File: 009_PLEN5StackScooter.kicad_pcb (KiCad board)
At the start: 2 copper layers, 0 parts

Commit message: [Add]インジケータLED追加
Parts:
- added BT1: Battery_Cell, 00_DIY_MyFavorite:BatteryHolder_BX123P38, F.Cu at (79.1, 61.2)
- added IC1: TB6608FNG_O,EL_, 01_AddLibrary:SOP65P640X160-20N, F.Cu at (80.6, 75.0)
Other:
- board outline added: 49.8 x 32 mm
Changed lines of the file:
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@@
   )
   (net 0 "")
+  (net 1 "+BATT")
+  (net 2 "GND")
+  (net 3 "VCC")
+  (net 4 "Standby")
+  (net 5 "Net-(IC1-OSC)")
+  (net 6 "Direction")
+  (net 7 "MotorB2")
+  (net 8 "Net-(IC1-RFB)")
+  (net 9 "MotorB1")
+  (net 10 "MotorA2")
+  (net 11 "Net-(IC1-RFA)")
+  (net 12 "MotorA1")
+  (net 13 "Reset")
+  (net 14 "unconnected-(IC1-~{MO}-Pad16)")
+  (net 15 "Enable")
+  (net 16 "Clock")
+  (footprint "00_DIY_MyFavorite:BatteryHolder_BX123P38" (layer "F.Cu")
+    (at 79.094 61.214)
+    (property "Sheetfile" "009_PLEN5StackScooter.kicad_sch")
+    (property "Sheetname" "")
+    (property "ki_description" "Single-cell battery")
+    (property "ki_keywords" "battery cell")
+    (attr through_hole)
+    (fp_text reference "BT1" (at 19 0 unlocked) (layer "F.SilkS")
+        (effects (font (size 1 1) (thickness 0.15)))
+    )
+    (fp_text value "Battery_Cell" (at 19 4 unlocked) (layer "F.Fab")
+        (effects (font (size 1 1) (thickness 0.15)))
+    )
+    (fp_text user "-" (at 35 -1 unlocked) (layer "F.SilkS")
+        (effects (font (size 1.5 1.5) (thickness 0.15)) (justify left bottom))
+    )
+    (fp_text user "+" (at 1 -1 unlocked) (layer "F.SilkS")
+        (effects (font (size 1.5 1.5) (thickness 0.15)) (justify left bottom))
+    )
+    (fp_rect (start -2.4 -9) (end 40.4 9)
+      (stroke (width 0.12) (type default)) (fill none) (layer "F.SilkS"))
+    (fp_circle (center 0 -8.2) (end 0.9 -8.2)
+      (stroke (width 0.12) (type default)) (fill none) (layer "Edge.Cuts"))
+    (pad "1" thru_hole circle (at 0 0) (size 2 2) (drill 1.4) (layers "*.Cu" "*.Mask")
+      (net 1 "+BATT") (pinfunction "+") (pintype "passive"))
+    (pad "2" thru_hole circle (at 38 0) (size 2 2) (drill 1.4) (layers "*.Cu" "*.Mask")
+      (net 2 "GND") (pinfunction "-") (pintype "passive"))
+    (model ":LIB:00_DIY_MyFavorite/3dmodels/BatteryHolder_BX123P38.STEP"
+      (offset (xyz 0 0 0))
+      (scale (xyz 1 1 1))
+      (rotate (xyz -90 0 0))
+    )
+  )
+  (footprint "01_AddLibrary:SOP65P640X160-20N" (layer "F.Cu")
+    (at 80.634 75.049)
+    (descr "SSOP20-P-225-0.65A")
+    (tags "Integrated Circuit")
+    (property "Height" "1.6")
+    (property "Manufacturer_Name" "Toshiba")
+    (property "Manufacturer_Part_Number" "TB6608FNG(O,EL)")
+    (property "RS Part Number" "")
+    (property "RS Price/Stock" "")
+    (property "Sheetfile" "009_PLEN5StackScooter.kicad_sch")
+    (property "Sheetname" "")
+    (property "ki_description" "Motor / Motion / Ignition Controllers & Drivers Stepping Motor Driver")
+    (attr smd)
+    (fp_text reference "IC1" (at 0 0) (layer "F.SilkS")
+        (effects (font (size 1.27 1.27) (thickness 0.254)))
+    )
+    (fp_text value "TB6608FNG_O,EL_" (at 0 0) (layer "F.SilkS") hide
+        (effects (font (size 1.27 1.27) (thickness 0.254)))
+    )
+    (fp_text user "${REFERENCE}" (at 0 0) (layer "F.Fab")
+        (effects (font (size 1.27 1.27) (thickness 0.254)))
+    )
+    (fp_line (start -3.725 -3.5) (end -2.2 -3.5)
+      (stroke (width 0.2) (type solid)) (layer "F.SilkS"))
+    (fp_line (start -1.85 -3.5) (end 1.85 -3.5)
+      (stroke (width 0.2) (type solid)) (layer "F.SilkS"))
+    (fp_line (start -1.85 3.5) (end -1.85 -3.5)
+      (stroke (width 0.2) (type solid)) (layer "F.SilkS"))
+    (fp_line (start 1.85 -3.5) (end 1.85 3.5)
+      (stroke (width 0.2) (type solid)) (layer "F.SilkS"))
+    (fp_line (start 1.85 3.5) (end -1.85 3.5)
+      (stroke (width 0.2) (type solid)) (layer "F.SilkS"))
+    (fp_line (start -3.975 -3.75) (end 3.975 -3.75)
+      (stroke (width 0.05) (type solid)) (layer "F.CrtYd"))
+    (fp_line (start -3.975 3.75) (end -3.975 -3.75)
+      (stroke (width 0.05) (type solid)) (layer "F.CrtYd"))
+    (fp_line (start 3.975 -3.75) (end 3.975 3.75)
+      (stroke (width 0.05) (type solid)) (layer "F.CrtYd"))
+    (fp_line (start 3.975 3.75) (end -3.975 3.75)
+      (stroke (width 0.05) (type solid)) (layer "F.CrtYd"))
+    (fp_line (start -2.2 -3.5) (end 2.2 -3.5)
+      (stroke (width 0.1) (type solid)) (layer "F.Fab"))
+    (fp_line (start -2.2 -2.85) (end -1.55 -3.5)
+      (stroke (width 0.1) (type solid)) (layer "F.Fab"))
+    (fp_line (start -2.2 3.5) (end -2.2 -3.5)
+      (stroke (width 0.1) (type solid)) (layer "F.Fab"))
+    (fp_line (start 2.2 -3.5) (end 2.2 3.5)
+      (stroke (width 0.1) (type solid)) (layer "F.Fab"))
+    (fp_line (start 2.2 3.5) (end -2.2 3.5)
+      (stroke (width 0.1) (type solid)) (layer "F.Fab"))
+    (pad "1" smd rect (at -2.962 -2.925 90) (size 0.45 1.525) (layers "F.Cu" "F.Paste" "F.Mask")
+      (net 3 "VCC") (pinfunction "VCC") (pintype "passive"))
+    (pad "2" smd rect (at -2.962 -2.275 90) (size 0.45 1.525) (layers "F.Cu" "F.Paste" "F.Mask")
+      (net 4 "Standby") (pinfunction "STBY") (pintype "passive"))
+    (pad "3" smd rect (at -2.962 -1.625 90) (size 0.45 1.525) (layers "F.Cu" "F.Paste" "F.Mask")
+      (net 5 "Net-(IC1-OSC)") (pinfunction "OSC") (pintype "passive"))
+    (pad "4" smd rect (at -2.962 -0.975 90) (size 0.45 1.525) (layers "F.Cu" "F.Paste" "F.Mask")
+      (net 3 "VCC") (pinfunction "M1") (pintype "passive"))
+    (pad "5" smd rect (at -2.962 -0.325 90) (size 0.45 1.525) (layers "F.Cu" "F.Paste" "F.Mask")
+      (net 2 "GND") (pinfunction "M2") (pintype "passive"))
+    (pad "6" smd rect (at -2.962 0.325 90) (size 0.45 1.525) (layers "F.Cu" "F.Paste" "F.Mask")
+      (net 1 "+BATT") (pinfunction "VM") (pintype "passive"))
+    (pad "7" smd rect (at -2.962 0.975 90) (size 0.45 1.525) (layers "F.Cu" "F.Paste" "F.Mask")
+      (net 6 "Direction") (pinfunction "CW/CCW") (pintype "passive"))
+    (pad "8" smd rect (at -2.962 1.625 90) (size 0.45 1.525) (layers "F.Cu" "F.Paste" "F.Mask")
+      (net 7 "MotorB2") (pinfunction "BO2") (pintype "passive"))
+    (pad "9" smd rect (at -2.962 2.275 90) (size 0.45 1.525) (layers "F.Cu" "F.Paste" "F.Mask")
+      (net 8 "Net-(IC1-RFB)") (pinfunction "RFB") (pintype "passive"))
+    (pad "10" smd rect (at -2.962 2.925 90) (size 0.45 1.525) (layers "F.Cu" "F.Paste" "F.Mask")
+      (net 9 "MotorB1") (pinfunction "BO1") (pintype "passive"))
+    (pad "11" smd rect (at 2.962 2.925 90) (size 0.45 1.525) (layers "F.Cu" "F.Paste" "F.Mask")
+      (net 10 "MotorA2") (pinfunction "AO2") (pintype "passive"))
+    (pad "12" smd rect (at 2.962 2.275 90) (size 0.45 1.525) (layers "F.Cu" "F.Paste" "F.Mask")
+      (net 11 "Net-(IC1-RFA)") (pinfunction "RFA") (pintype "passive"))
+    (pad "13" smd rect (at 2.962 1.625 90) (size 0.45 1.525) (layers "F.Cu" "F.Paste" "F.Mask")
+      (net 12 "MotorA1") (pinfunction "AO1") (pintype "passive"))
+    (pad "14" smd rect (at 2.962 0.975 90) (size 0.45 1.525) (layers "F.Cu" "F.Paste" "F.Mask")
+      (net 13 "Reset") (pinfunction "RESET") (pintype "passive"))
+    (pad "15" smd rect (at 2.962 0.325 90) (size 0.45 1.525) (layers "F.Cu" "F.Paste" "F.Mask")
+      (net 2 "GND") (pinfunction "GND") (pintype "passive"))
+    (pad "16" smd rect (at 2.962 -0.325 90) (size 0.45 1.525) (layers "F.Cu" "F.Paste" "F.Mask")
+      (net 14 "unconnected-(IC1-~{MO}-Pad16)") (pinfunction "~{MO}") (pintype "passive+no_connect"))
+    (pad "17" smd rect (at 2.962 -0.975 90) (size 0.45 1.525) (layers "F.Cu" "F.Paste" "F.Mask")
+      (net 2 "GND") (pinfunction "TQ") (pintype "passive"))
+    (pad "18" smd rect (at 2.962 -1.625 90) (size 0.45 1.525) (layers "F.Cu" "F.Paste" "F.Mask")
+      (net 2 "GND") (pinfunction "DCY") (pintype "passive"))
+    (pad "19" smd rect (at 2.962 -2.275 90) (size 0.45 1.525) (layers "F.Cu" "F.Paste" "F.Mask")
+      (net 15 "Enable") (pinfunction "ENABLE") (pintype "passive"))
+    (pad "20" smd rect (at 2.962 -2.925 90) (size 0.45 1.525) (layers "F.Cu" "F.Paste" "F.Mask")
+      (net 16 "Clock") (pinfunction "CK") (pintype "passive"))
+    (model ":LIB:PCBL/SamacSys_Parts.3dshapes/TB6608FNG,C8,EL.stp"
+      (offset (xyz 0 0 0))
+      (scale (xyz 1 1 1))
+      (rotate (xyz 0 0 0))
+    )
+  )
+  (gr_rect (start 73.914 50.038) (end 123.698 82.042)
+    (stroke (width 0.1) (type default)) (fill none) (layer "Edge.Cuts"))
 )

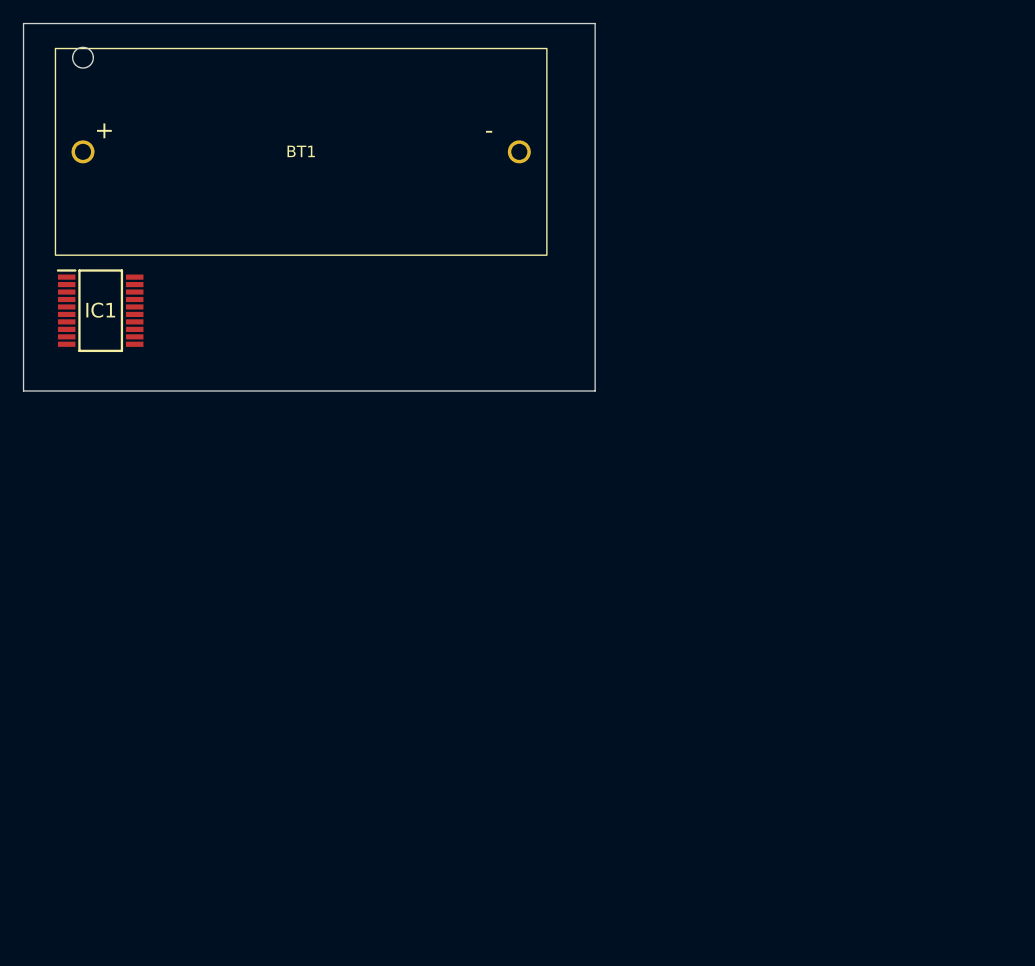
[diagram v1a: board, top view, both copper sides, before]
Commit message: [Add]モータ2台分のドライバIC追加
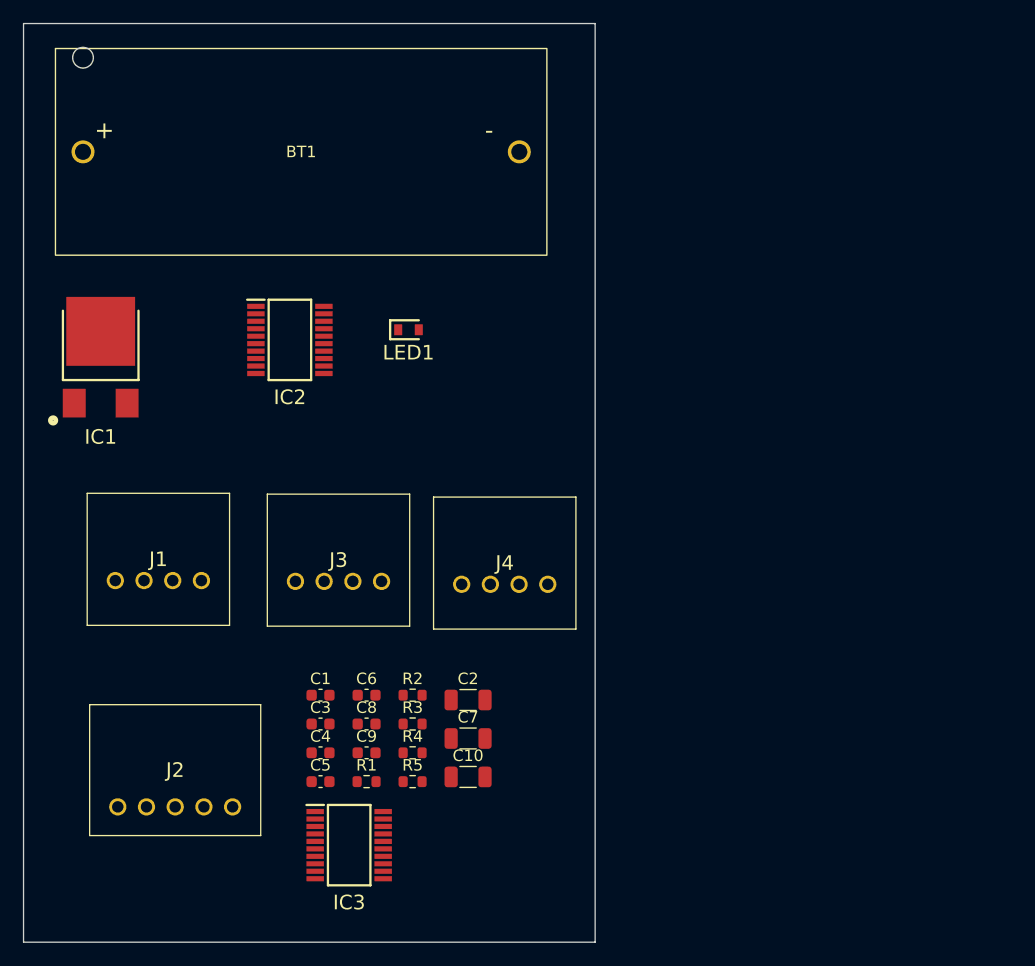
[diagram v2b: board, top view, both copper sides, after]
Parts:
- added C1: 0.1u, Capacitor_SMD:C_0603_1608Metric, F.Cu at (99.8, 108.5)
- added C10: 100u, Capacitor_SMD:C_1206_3216Metric, F.Cu at (112.6, 115.7)
- added C2: 100u, Capacitor_SMD:C_1206_3216Metric, F.Cu at (112.6, 109.0)
- added C3: 0.33u, Capacitor_SMD:C_0603_1608Metric, F.Cu at (99.8, 111.0)
- added C4: 2.2u, Capacitor_SMD:C_0603_1608Metric, F.Cu at (99.8, 113.6)
- added C5: C, Capacitor_SMD:C_0603_1608Metric, F.Cu at (99.8, 116.1)
- added C6: 0.1u, Capacitor_SMD:C_0603_1608Metric, F.Cu at (103.8, 108.5)
- added C7: 100u, Capacitor_SMD:C_1206_3216Metric, F.Cu at (112.6, 112.3)
- added C8: C, Capacitor_SMD:C_0603_1608Metric, F.Cu at (103.8, 111.0)
- added C9: 0.1u, Capacitor_SMD:C_0603_1608Metric, F.Cu at (103.8, 113.6)
- added IC2: TB6608FNG_O,EL_, 01_AddLibrary:SOP65P640X160-20N, F.Cu at (97.1, 77.6)
- added IC3: TB6608FNG_O,EL_, 01_AddLibrary:SOP65P640X160-20N, F.Cu at (102.3, 121.6)
- added J1: S4B-XH-A-1_LF__SN_, 01_AddLibrary:S4BXHA1LFSN, F.Cu at (81.9, 98.6)
- added J2: S5B-XH-A-1_LF__SN_, 01_AddLibrary:S5BXHA1LFSN, F.Cu at (92.1, 118.3)
- added J3: S4B-XH-A-1_LF__SN_, 01_AddLibrary:S4BXHA1LFSN, F.Cu at (97.6, 98.6)
- added J4: S4B-XH-A-1_LF__SN_, 01_AddLibrary:S4BXHA1LFSN, F.Cu at (112.1, 98.9)
- added LED1: SML-E12P8WT86, 01_AddLibrary:LEDC1608X36N, F.Cu at (107.4, 76.7)
- added R1: 1k, Resistor_SMD:R_0603_1608Metric, F.Cu at (103.8, 116.1)
- added R2: 2.2, Resistor_SMD:R_0603_1608Metric, F.Cu at (107.8, 108.5)
- added R3: 2.2, Resistor_SMD:R_0603_1608Metric, F.Cu at (107.8, 111.0)
- added R4: 2.2, Resistor_SMD:R_0603_1608Metric, F.Cu at (107.8, 113.6)
- added R5: 2.2, Resistor_SMD:R_0603_1608Metric, F.Cu at (107.8, 116.1)
- IC1: value TB6608FNG_O,EL_ -> NJM2845DL1-33-TE1; footprint 01_AddLibrary:SOP65P640X160-20N -> 01_AddLibrary:TO-252-3-L1
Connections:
- IC1 pad 1: VCC -> +BATT
- IC1 pad 2: Standby -> +3.3V
- IC1 pad 3: Net-(IC1-OSC) -> GND
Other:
- board size 49.8 x 32 mm -> 49.8 x 80 mm

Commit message: [Add]ステッピングモータテスト用基板設計完
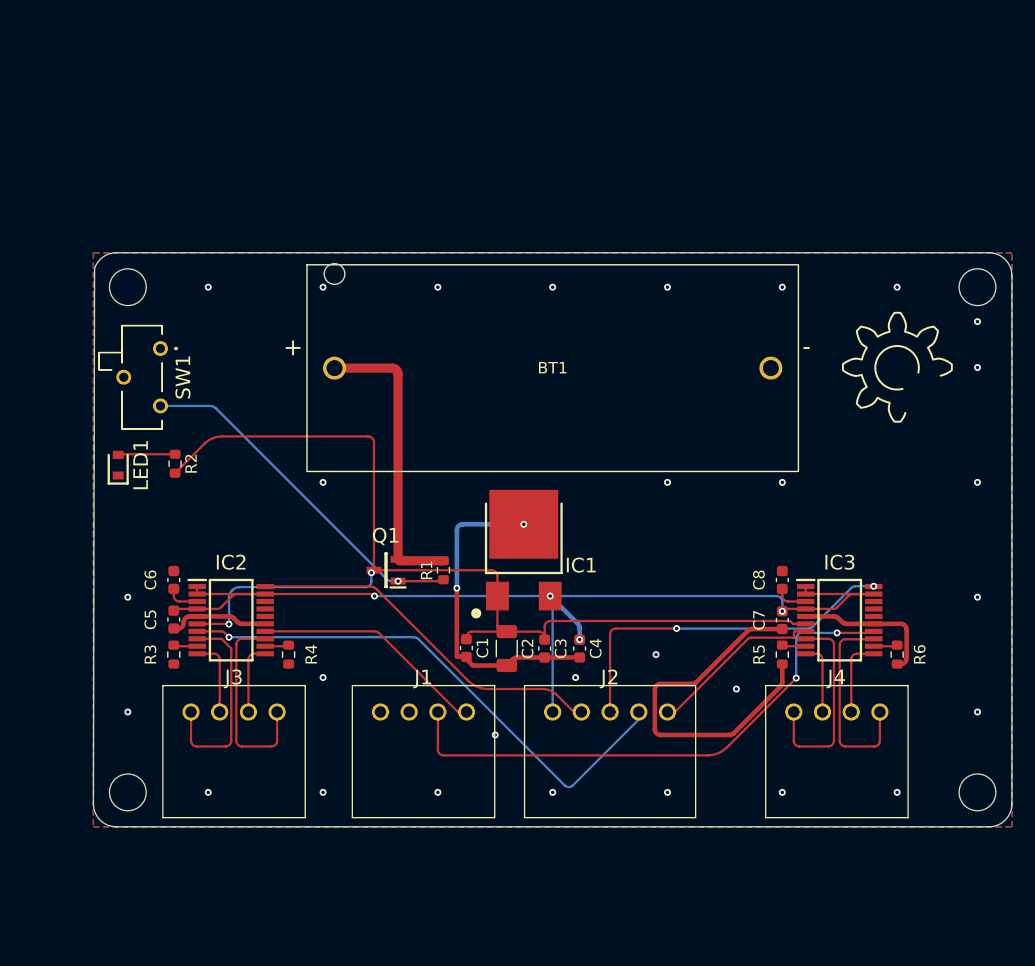
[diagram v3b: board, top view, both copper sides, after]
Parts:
- removed C10: 100u, Capacitor_SMD:C_1206_3216Metric
- removed C9: 0.1u, Capacitor_SMD:C_0603_1608Metric
- added G***: LOGO, 00_DIY_MyFavorite:Symbol_Helical_new, F.Cu at (150.0, 80.0)
- added Q1: IRLML6402, 01_AddLibrary:SOT95P237X112-3N, F.Cu at (105.5, 97.7)
- added R6: 2.2, Resistor_SMD:R_0603_1608Metric, F.Cu at (150.0, 105.0)
- added Ref**: Val**, 10_KBD_Hole_salicylic:m3_Screw_Hole_EdgeCuts, F.Cu at (157.0, 73.0)
- added Ref**: Val**, 10_KBD_Hole_salicylic:m3_Screw_Hole_EdgeCuts, F.Cu at (83.0, 117.0)
- added Ref**: Val**, 10_KBD_Hole_salicylic:m3_Screw_Hole_EdgeCuts, F.Cu at (83.0, 73.0)
- added Ref**: Val**, 10_KBD_Hole_salicylic:m3_Screw_Hole_EdgeCuts, F.Cu at (157.0, 117.0)
- added SW1: SW_OTAX-Toggle, 01_AddLibrary:IS1245TG, F.Cu at (85.8, 78.3)
- C5: value C -> 0.1u
- C6: value 0.1u -> 220p
- C7: value 100u -> 0.1u; footprint Capacitor_SMD:C_1206_3216Metric -> Capacitor_SMD:C_0603_1608Metric
- C8: value C -> 220p
- R2: value 2.2 -> 1k
- moved IC3 47.0 mm to (145.0, 102.0)
- moved IC1 40.5 mm to (117.5, 91.9)
- moved C8 38.3 mm to (140.0, 98.5), turned to 90 degrees
- moved J4 38.1 mm to (148.5, 110.0), turned to 180 degrees
- moved R5 34.0 mm to (140.0, 105.0), turned to -90 degrees
- moved J1 32.7 mm to (112.5, 110.0), turned to 180 degrees
- moved C7 29.2 mm to (140.0, 102.0), turned to -90 degrees
- moved J2 29.1 mm to (120.0, 110.0), turned to 180 degrees
- moved BT1 28.9 mm to (101.0, 80.0)
- moved R2 28.9 mm to (87.1, 88.4), turned to -90 degrees
- moved LED1 27.9 mm to (82.2, 88.5), turned to 90 degrees
- moved IC2 24.9 mm to (92.0, 102.0)
- moved C4 24.3 mm to (122.3, 104.5), turned to -90 degrees
- moved R3 21.7 mm to (87.0, 105.0), turned to -90 degrees
- moved C3 20.6 mm to (119.3, 104.5), turned to -90 degrees
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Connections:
- BT1 pad 1: +BATT -> /Power
- C5 pad 1: Net-(IC2-OSC) -> +3.3V
- C6 pad 1: +3.3V -> Net-(IC2-OSC)
- IC2 pad 17: GND -> unconnected-(IC2-TQ-Pad17)
- IC2 pad 18: GND -> unconnected-(IC2-DCY-Pad18)
- IC2 pad 19: Enable_1 -> +3.3V
- IC2 pad 2: Standby_1 -> +3.3V
- IC3 pad 17: GND -> unconnected-(IC3-TQ-Pad17)
- IC3 pad 18: GND -> unconnected-(IC3-DCY-Pad18)
- IC3 pad 19: Enable_2 -> +3.3V
- IC3 pad 2: Standby_2 -> +3.3V
- J1 pad 1: unconnected-(J1-Pad1) -> Reset_1
- J1 pad 2: unconnected-(J1-Pad2) -> Reset_2
- J1 pad 4: unconnected-(J1-Pad4) -> GND
- J2 pad 1: unconnected-(J2-Pad1) -> +3.3V
- J2 pad 2: unconnected-(J2-Pad2) -> Clock_1
- J2 pad 3: unconnected-(J2-Pad3) -> Clock_2
- J2 pad 4: unconnected-(J2-Pad4) -> Direction_1
- J2 pad 5: unconnected-(J2-Pad5) -> Direction_2
- R1 pad 1: Net-(LED1-A) -> Net-(Q1-G)
- R1 pad 2: +BATT -> /Power
- R2 pad 1: Net-(IC2-RFB) -> Net-(LED1-A)
- R2 pad 2: GND -> +BATT
- R3 pad 1: Net-(IC2-RFA) -> Net-(IC2-RFB)
- R4 pad 1: Net-(IC3-RFB) -> Net-(IC2-RFA)
- R5 pad 1: Net-(IC3-RFA) -> Net-(IC3-RFB)
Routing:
- net +BATT: track 0.00 -> 97.4 mm, vias 0 -> 2
- net +3.3V: track 0.00 -> 91.3 mm, vias 0 -> 4
- net GND: track 0.00 -> 82.3 mm, vias 0 -> 31
- net Reset_2: track 0.00 -> 47.9 mm, vias 0 -> 2
- net Direction_1: track 0.00 -> 47.1 mm, vias 0 -> 1
- net Clock_1: track 0.00 -> 31.8 mm
- net Clock_2: track 0.00 -> 31.5 mm, vias 0 -> 2
- net Net-(Q1-G): track 0.00 -> 30.9 mm, vias 0 -> 1
- net /Power: track 0.00 -> 26.0 mm
- net Reset_1: track 0.00 -> 20.4 mm
- net MotorA3: track 0.00 -> 18.1 mm
- net MotorB2: track 0.00 -> 17.9 mm
- net MotorA1: track 0.00 -> 17.8 mm
- net MotorB4: track 0.00 -> 17.6 mm
- net Direction_2: track 0.00 -> 15.2 mm
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- added copper zone on B.Cu, net GND
- added copper zone on F.Cu, net GND
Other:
- board size 49.8 x 80 mm -> 80 x 50 mm
- board text added: "JLCJLCJLCJLC"
- board text added: "PLEN5StackScooter_TestBoard v1.0"

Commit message: [Add]最終レイアウトに近い基板設計完
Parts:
- removed the Ref** at (157.0, 73.0)
- removed the Ref** at (83.0, 117.0)
- removed the Ref** at (83.0, 73.0)
- removed the Ref** at (157.0, 117.0)
- added D1: CUHS20F30,H3F, 01_AddLibrary:CUHS20F30H3F, F.Cu at (139.0, 78.0)
- added Ref**: Val**, 10_KBD_Hole_salicylic:m3_Screw_Hole_EdgeCuts, F.Cu at (156.0, 116.0)
- added Ref**: Val**, 10_KBD_Hole_salicylic:m3_Screw_Hole_EdgeCuts, F.Cu at (84.0, 64.0)
- added Ref**: Val**, 10_KBD_Hole_salicylic:m3_Screw_Hole_EdgeCuts, F.Cu at (156.0, 64.0)
- added Ref**: Val**, 10_KBD_Hole_salicylic:m3_Screw_Hole_EdgeCuts, F.Cu at (84.0, 116.0)
- moved SW1 57.7 mm to (142.5, 67.2), turned to 180 degrees
- moved LED1 54.6 mm to (131.0, 64.0), turned to 180 degrees
- moved R2 48.4 mm to (131.0, 68.0), turned to 0 degrees
- moved R1 27.9 mm to (107.0, 70.0), turned to 180 degrees
- moved IC1 27.7 mm to (119.0, 64.2)
- moved C3 26.5 mm to (120.0, 78.0)
- moved C4 26.5 mm to (123.0, 78.0)
- moved C2 26.5 mm to (116.0, 78.0)
- moved C1 26.4 mm to (112.0, 78.0)
- moved J4 23.8 mm to (149.6, 86.2), turned to -90 degrees
- moved Q1 21.7 mm to (107.0, 76.0), turned to -90 degrees
- moved J3 17.2 mm to (90.5, 93.8), turned to 90 degrees
- moved BT1 11.0 mm to (101.0, 91.0)
- moved R5 6.40 mm to (145.0, 109.0)
- moved C7 5.83 mm to (145.0, 105.0)
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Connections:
- BT1 pad 2: GND -> Net-(BT1--)
- IC2 pad 17: unconnected-(IC2-TQ-Pad17) -> +3.3V
- IC3 pad 17: unconnected-(IC3-TQ-Pad17) -> +3.3V
- J1 pad 2: Reset_2 -> Direction_1
- J2 pad 4: Direction_1 -> Reset_2
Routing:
- net +3.3V: track 91.3 -> 172.4 mm, vias 4 -> 0
- net GND: track 82.3 -> 40.1 mm, vias 31 -> 32
- net +BATT: track 97.4 -> 125.2 mm, vias 2 -> 3
- net Net-(Q1-G): track 30.9 -> 50.2 mm, vias 1 -> 0
- net MotorA2: track 6.30 -> 23.5 mm, vias 0 -> 1
- net MotorB3: track 6.30 -> 23.4 mm, vias 0 -> 1
- net Net-(BT1--): track 0.00 -> 13.5 mm
- net Direction_1: track 47.1 -> 33.8 mm, vias 1 -> 0
- net MotorA4: track 6.80 -> 20.1 mm, vias 0 -> 1
- net MotorB1: track 6.80 -> 19.5 mm, vias 0 -> 1
- net Reset_2: track 47.9 -> 35.3 mm, vias 2 -> 0
- net Clock_2: track 31.5 -> 41.5 mm, vias 2 -> 0
- net MotorB4: track 17.6 -> 24.9 mm, vias 0 -> 1
- net MotorA1: track 17.8 -> 24.7 mm, vias 0 -> 1
- net Reset_1: track 20.4 -> 13.5 mm
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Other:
- board size 80 x 50 mm -> 80 x 60 mm
- board text added: "PLEN5StackScooter_TestBoard v2.0"
- board text removed: "PLEN5StackScooter_TestBoard v1.0"
